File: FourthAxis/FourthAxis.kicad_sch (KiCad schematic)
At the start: 31 parts, among them J1 36V, J2 DRIVER_CONN, J3 ENC_CONN, J4 HW_CONN, J5 SCREEN_CONN, J6 PROG_HEADER, SW29 BOOT, SW30 RESET, U1 ESP32-WROOM-32

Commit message: started routing
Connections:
- net PROG_RX renamed PROG_N
- net PROG_TX renamed PROG_P
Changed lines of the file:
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@@
 		)
 	)
-	(global_label "PROG_RX"
+	(global_label "PROG_N"
 		(shape bidirectional)
 		(at 151.13 66.04 0)
@@
 		)
 		(property "Intersheetrefs" "${INTERSHEET_REFS}"
-			(at 163.0011 66.04 0)
+			(at 161.8521 66.04 0)
 			(hide yes)
 			(show_name no)
@@
 		)
 	)
-	(global_label "PROG_RX"
+	(global_label "PROG_N"
 		(shape bidirectional)
 		(at 59.69 116.84 180)
@@
 		)
 		(property "Intersheetrefs" "${INTERSHEET_REFS}"
-			(at 47.8189 116.84 0)
+			(at 48.9679 116.84 0)
 			(hide yes)
 			(show_name no)
@@
 		)
 	)
-	(global_label "PROG_TX"
+	(global_label "PROG_P"
 		(shape bidirectional)
 		(at 151.13 60.96 0)
@@
 		)
 		(property "Intersheetrefs" "${INTERSHEET_REFS}"
-			(at 162.6987 60.96 0)
+			(at 161.7916 60.96 0)
 			(hide yes)
 			(show_name no)
@@
 		)
 	)
-	(global_label "PROG_TX"
+	(global_label "PROG_P"
 		(shape bidirectional)
 		(at 59.69 114.3 180)
@@
 		)
 		(property "Intersheetrefs" "${INTERSHEET_REFS}"
-			(at 48.1213 114.3 0)
-			(hide yes)
-			(show_name no)
+			(at 49.0284 114.3 0)
+			(hide yes)
+			(show_name no)

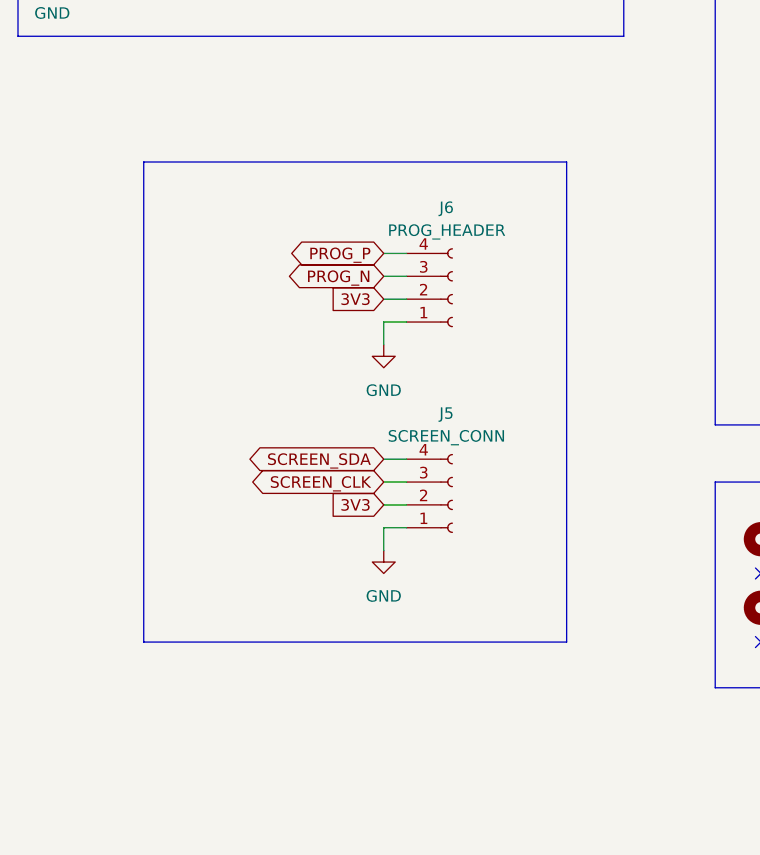
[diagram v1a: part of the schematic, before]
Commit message: traces almost complete
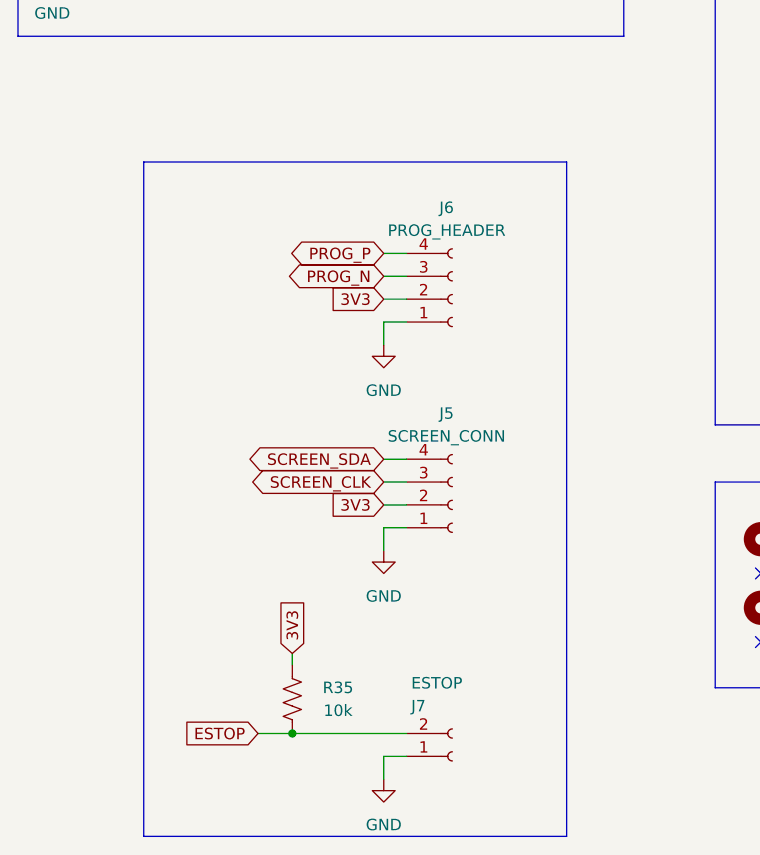
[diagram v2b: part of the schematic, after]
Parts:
- added J7: ESTOP, Connector_PinHeader_2.54mm:PinHeader_1x02_P2.54mm_Vertical, symbol Connector:Conn_01x02_Socket
- added R35: 10k, Resistor_SMD:R_0603_1608Metric, symbol Device:R_US
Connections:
- net 3V3: now also R35.1
- net ESTOP: now also J7.2 (Pin_2), R35.2
- net GND: now also J7.1 (Pin_1)

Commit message: BOM export
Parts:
- J1, J2, J3, J4, J5, J6, J7: now left out of the parts list
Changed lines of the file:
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@@
 		(body_style 1)
 		(exclude_from_sim no)
-		(in_bom yes)
+		(in_bom no)
 		(on_board yes)
 		(in_pos_files yes)
@@
 		(body_style 1)
 		(exclude_from_sim no)
-		(in_bom yes)
+		(in_bom no)
 		(on_board yes)
 		(in_pos_files yes)
@@
 		(body_style 1)
 		(exclude_from_sim no)
-		(in_bom yes)
+		(in_bom no)
 		(on_board yes)
 		(in_pos_files yes)
@@
 		(body_style 1)
 		(exclude_from_sim no)
-		(in_bom yes)
+		(in_bom no)
 		(on_board yes)
 		(in_pos_files yes)
@@
 		(body_style 1)
 		(exclude_from_sim no)
-		(in_bom yes)
+		(in_bom no)
 		(on_board yes)
 		(in_pos_files yes)
@@
 		(body_style 1)
 		(exclude_from_sim no)
-		(in_bom yes)
+		(in_bom no)
 		(on_board yes)
 		(in_pos_files yes)
@@
 		(body_style 1)
 		(exclude_from_sim no)
-		(in_bom yes)
+		(in_bom no)
 		(on_board yes)
 		(in_pos_files yes)

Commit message: boards ordered
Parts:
- C9: digikey 1276-1184-1-ND -> 1292-0603X106M100CT-ND
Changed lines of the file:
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@@
 			)
 		)
-		(property "digikey" "1276-1184-1-ND"
+		(property "digikey" "1292-0603X106M100CT-ND"
 			(at 160.02 41.91 0)
 			(hide yes)
